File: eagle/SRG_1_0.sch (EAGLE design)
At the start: 14 parts, among them IC1 74HC595N, X1 Serial Ctrl, X2 In Serial, X3 Out X, X4 Out Y, X5 Reg Ctrl

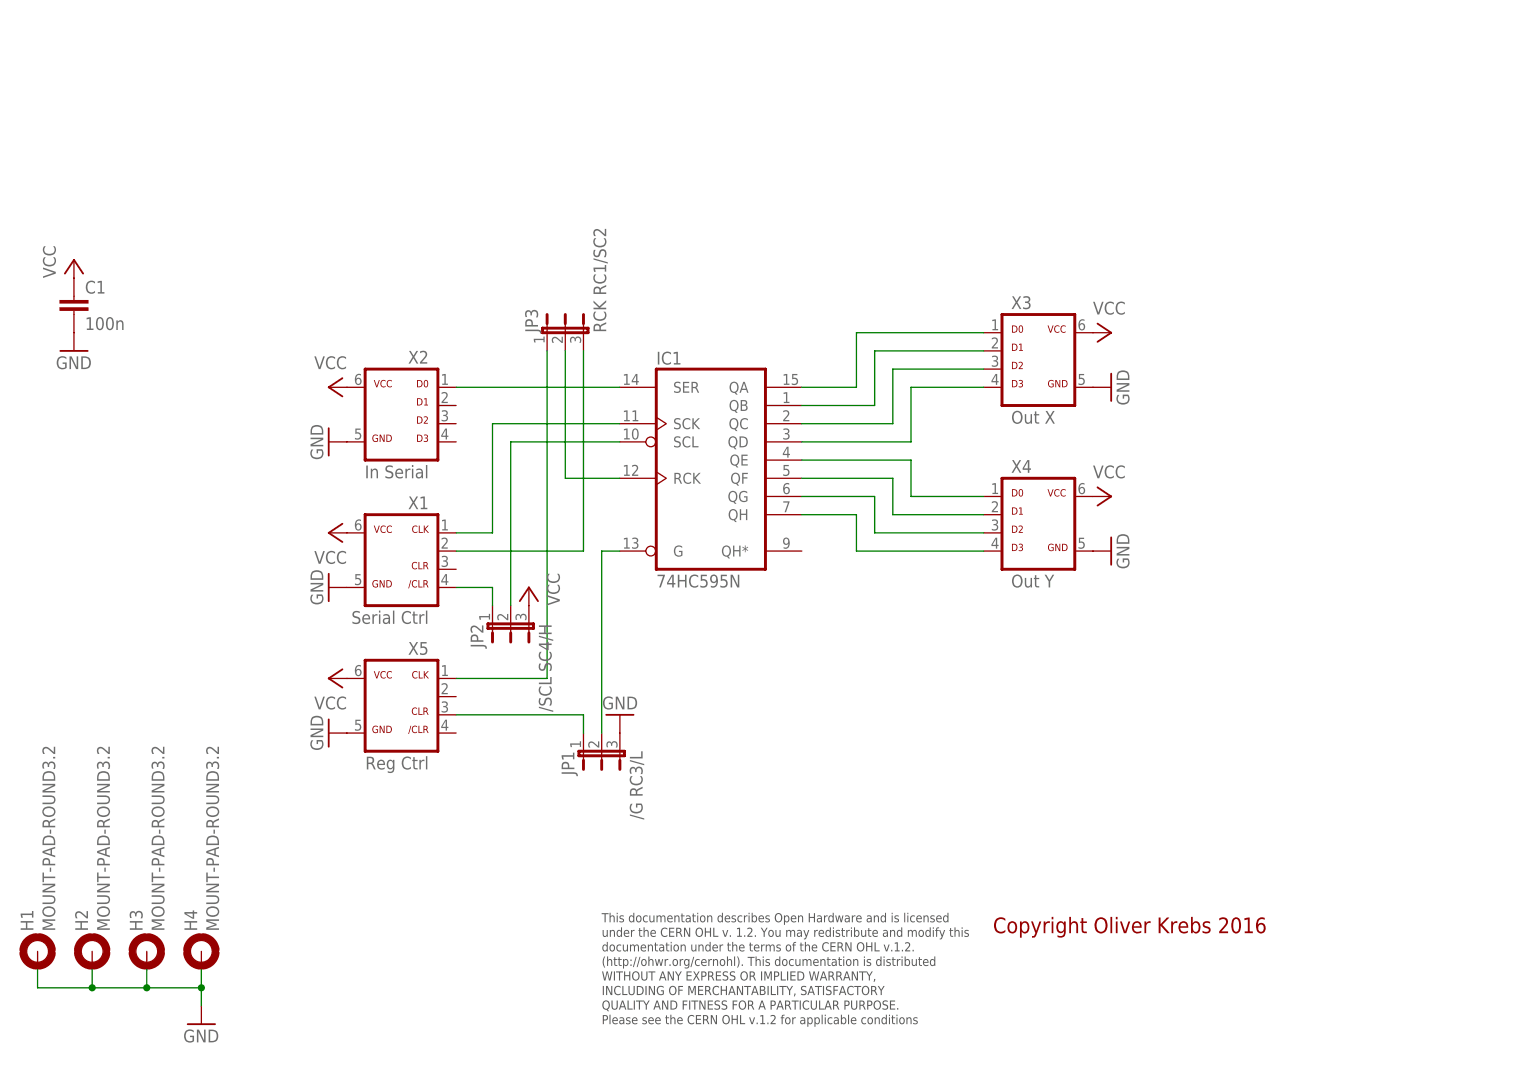
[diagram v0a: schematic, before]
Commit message: Add new tetra-Board and arduino files
Add AMP_1_0, AVC_1_0, D18_1_1, IOP_1_2, MIC_1_0, PIN_1_1, POT_1_0, PWA_1_0, PWR_1_0, RGF 2.0, SOC_2_0, VLT_1_0
Add mex_nano_shield_keyboard, mex_nano_shied_numbers

New arduino projects
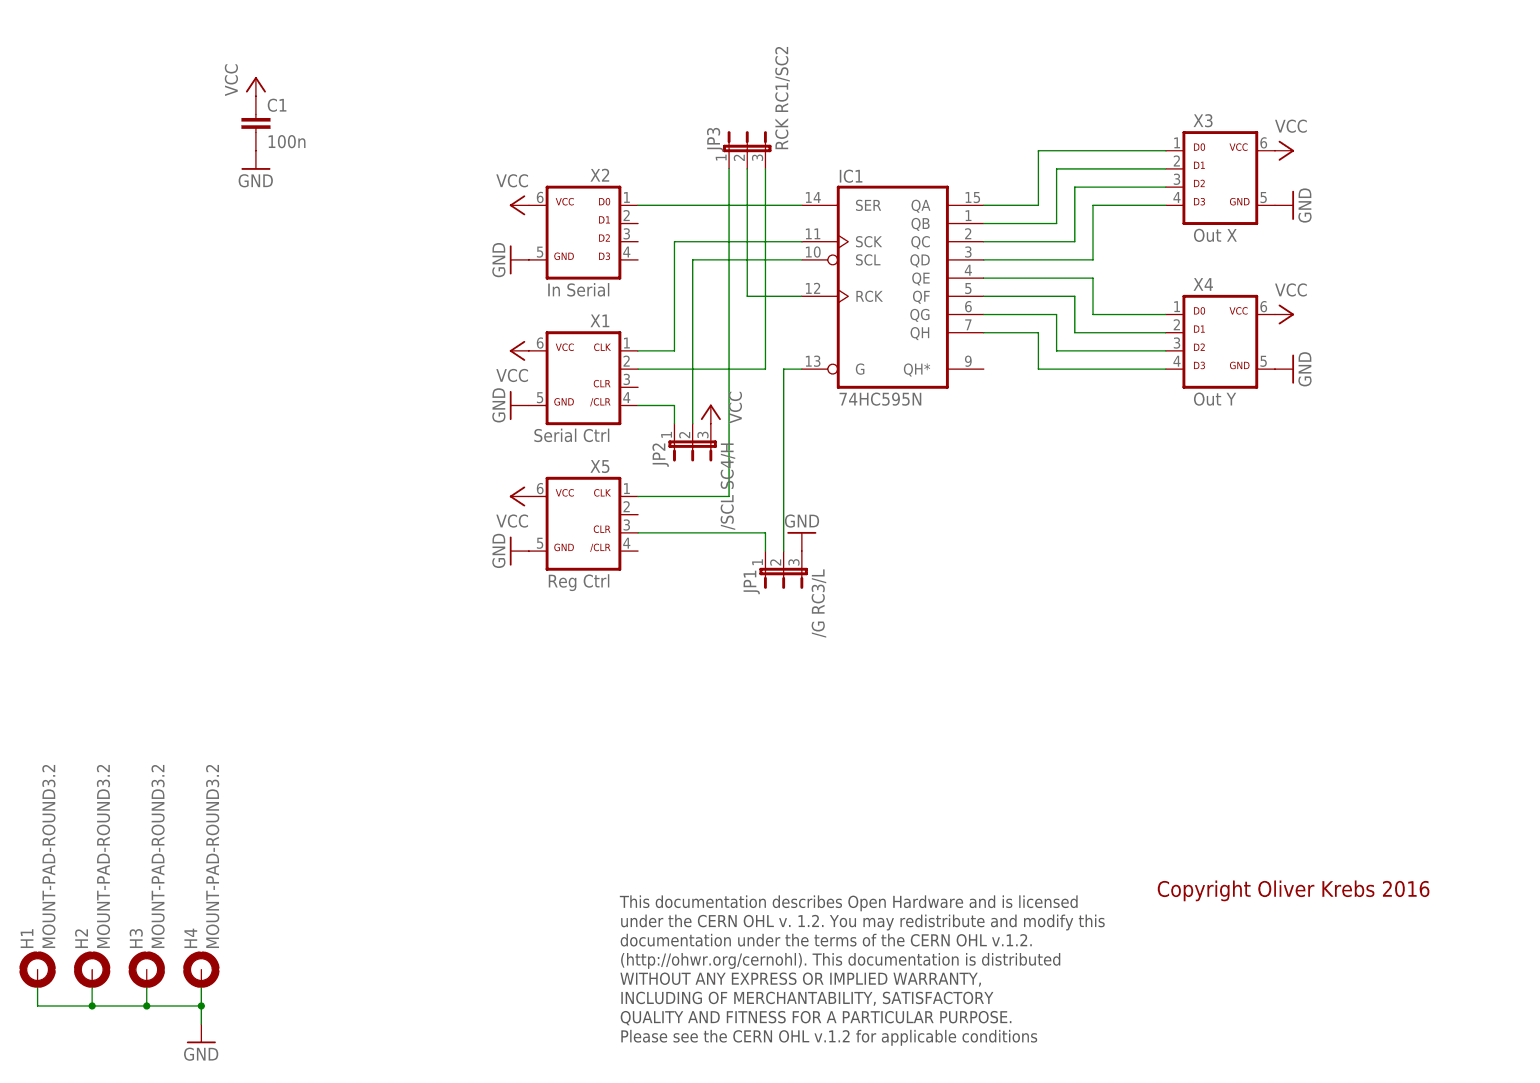
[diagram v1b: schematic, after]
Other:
- moved on the sheet: C1, H1, H2, H3, H4, IC1, JP1, JP2, JP3, X1, X2, X3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
